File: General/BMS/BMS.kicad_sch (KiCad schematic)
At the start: 25 parts, among them J1 CAN, J2 CAN, J3 DuraClik, J4 XT90, J5 XT90, J7 ExtPwrSw, K1 A3_Relay, Q1 PMV28ENEA, SW2 DBG2, SW3 DBG1, SW4 RST, U1 VXO7803

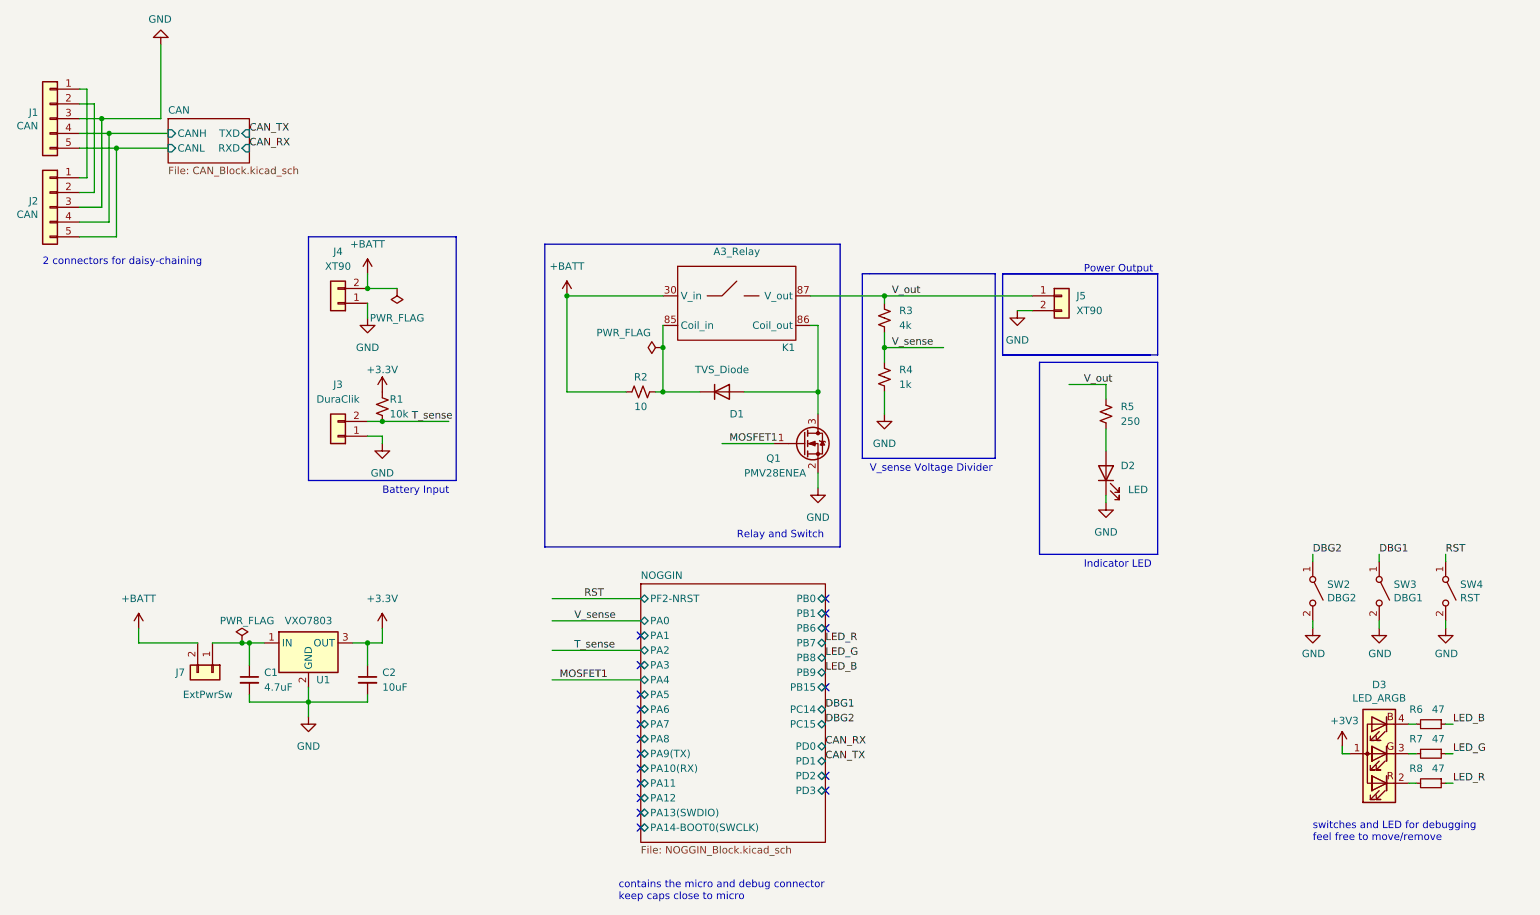
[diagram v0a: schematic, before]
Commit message: Changes: - added current sense to schematic - starting on layout
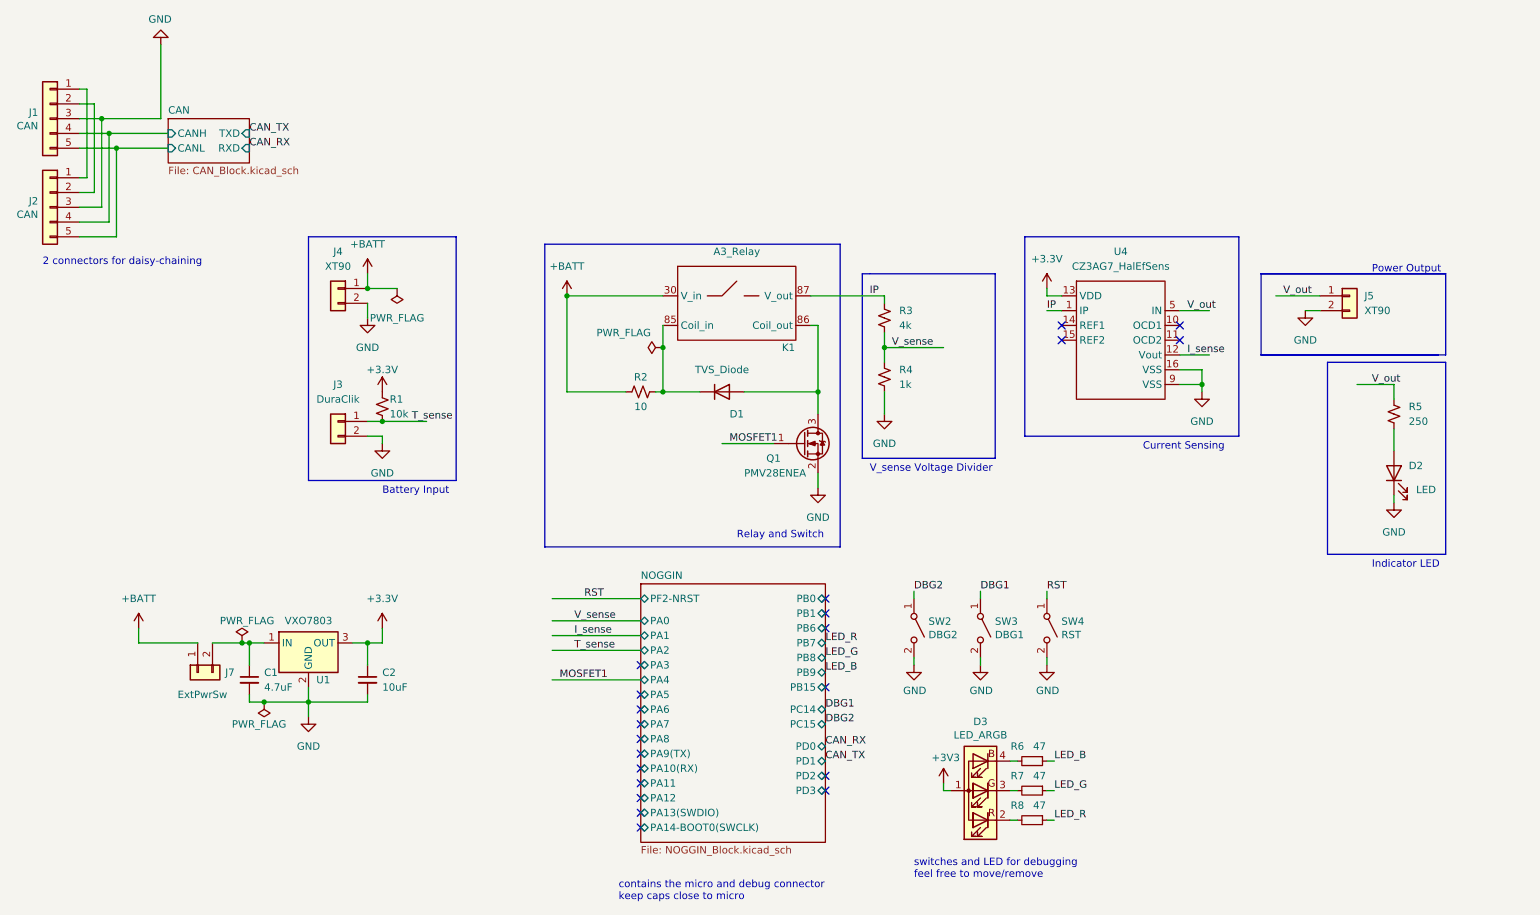
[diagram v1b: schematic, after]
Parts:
- added U4: CZ3AG7_HalEfSens, BMS_Library:CZ3AG7_HalEfSens, symbol BMS_Library:CZ3AG7_HalEfSens
- C1, C2: footprint (none) -> Capacitor_SMD:C_0603_1608Metric
- D1: footprint (none) -> Diode_SMD:D_SMC
- D2: footprint (none) -> LED_SMD:LED_Cree-PLCC4_2x2mm_CW
- J3, J7: footprint (none) -> extraparts:Molex_DuraClik_Vert_2pin
- J4, J5: footprint (none) -> BMS_Library:Conn_XT90
- K1: footprint (none) -> BMS_Library:A3_Relay
- Q1: footprint (none) -> Package_TO_SOT_SMD:SOT-23-5_HandSoldering
- R1, R2: footprint (none) -> Resistor_SMD:R_0805_2012Metric
- R3: footprint (none) -> Resistor_SMD:R_1206_3216Metric
- R4, R5: footprint (none) -> Resistor_SMD:R_0603_1608Metric
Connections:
- net +3V3: now also U4.13 (VDD)
- net +BATT: now also J4.1 (Pin_1), J7.1 (Pin_1); no longer J4.2 (Pin_2), J7.2 (Pin_2)
- net GND: now also J3.2 (Pin_2), J4.2 (Pin_2), U4.16 (VSS), U4.9 (VSS); no longer J3.1 (Pin_1), J4.1 (Pin_1)
- net T_sense: now also J3.1 (Pin_1); no longer J3.2 (Pin_2)
- net V_out: now also U4.5 (IN); no longer K1.87 (V_out), R3.2
- net at C1.1, U1.1 (IN): now also J7.2 (Pin_2); no longer J7.1 (Pin_1)
- new net IP: K1.87 (V_out), R3.2, U4.1 (IP)
- new net I_sense: U4.12 (Vout)
- no-connect marks 18 -> 21
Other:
- note added: "Current Sensing"
- moved on the sheet: D2, D3, J3, J4, J5, J7, R5, R6, R7, R8, SW2, SW3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
